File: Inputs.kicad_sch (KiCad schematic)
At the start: 6 parts, among them J26 Conn_01x04_Socket, J27 Conn_01x04_Socket, J28 Conn_01x04_Socket, J29 Conn_01x04_Socket, J30 Conn_01x02_Socket

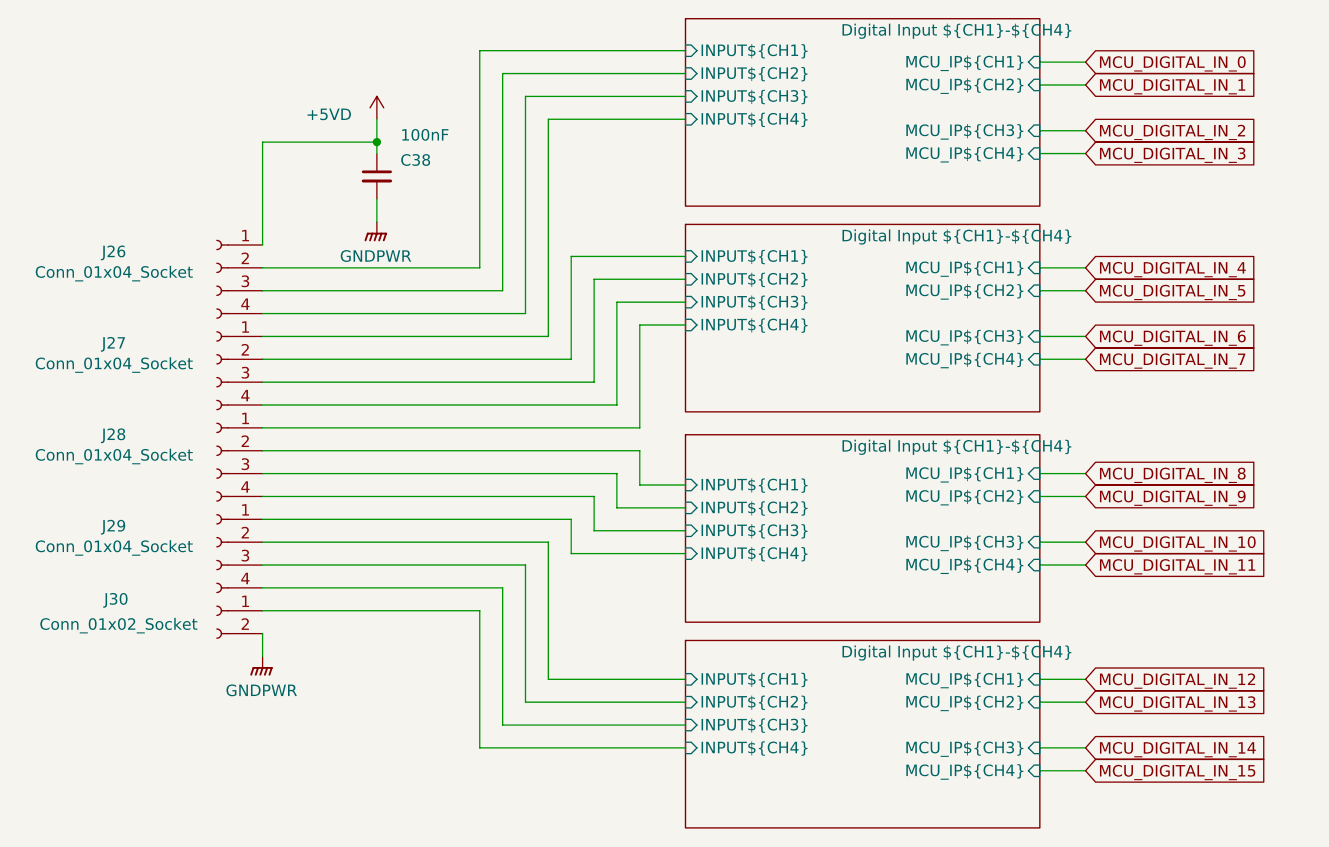
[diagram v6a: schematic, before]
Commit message: Switched terminal footprints over to a finer pitch. Corrected an issue with component reference values preventing proper use of multi channel rule areas. Component references for 4 channel optos are more straightforward as a result
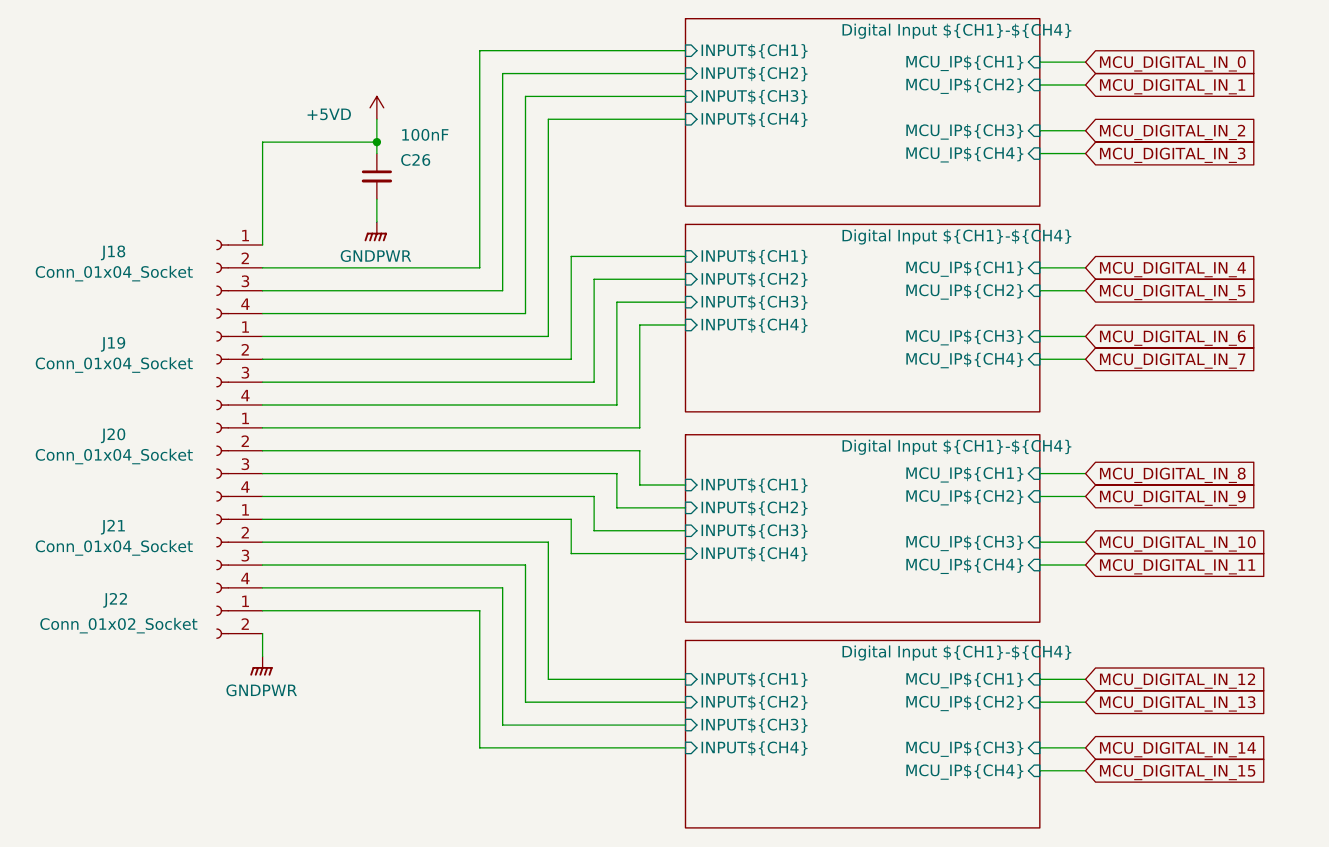
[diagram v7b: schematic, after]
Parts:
- J18: renamed from J26; footprint Amphenol QT:QT04ADP83V0000G -> 691412120004B:691412120004B; Digikey Part Number 1818-QT04ADP83V0000G-ND -> 732-691412120004B-ND; Digikey URL https://www.digikey.com.au/en/products/detail/amphenol-anyt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 -> https://www.digikey.com.au/en/products/detail/w%C3%BCrth-el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
- J19: renamed from J27; footprint Amphenol QT:QT04ADP83V0000G -> 691412120004B:691412120004B; Digikey Part Number 1818-QT04ADP83V0000G-ND -> 732-691412120004B-ND; Digikey URL https://www.digikey.com.au/en/products/detail/amphenol-anyt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 -> https://www.digikey.com.au/en/products/detail/w%C3%BCrth-el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
- J20: renamed from J28; footprint Amphenol QT:QT04ADP83V0000G -> 691412120004B:691412120004B; Digikey Part Number 1818-QT04ADP83V0000G-ND -> 732-691412120004B-ND; Digikey URL https://www.digikey.com.au/en/products/detail/amphenol-anyt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 -> https://www.digikey.com.au/en/products/detail/w%C3%BCrth-el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
- J21: renamed from J29; footprint Amphenol QT:QT04ADP83V0000G -> 691412120004B:691412120004B; Digikey Part Number 1818-QT04ADP83V0000G-ND -> 732-691412120004B-ND; Digikey URL https://www.digikey.com.au/en/products/detail/amphenol-anyt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 -> https://www.digikey.com.au/en/products/detail/w%C3%BCrth-el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
- J22: renamed from J30; footprint Amphenol QT:QT02ADP83V0000G -> 691412120002B:691412120002B; Digikey Part Number 1818-QT02ADP83V0000G-ND -> 732-691412120002B-ND; Digikey URL https://www.digikey.com.au/en/products/detail/amphenol-anyt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 -> https://www.digikey.com.au/en/products/detail/w%C3%BCrth-el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
- renumbered C38 to C26
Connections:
- net Digital Input ${CH1}-${CH4}/INPUT${CH1} is gone; now on net Digital Input ${CH1}-${CH4}/INPUT${CH1}: J19.2 (Pin_2)
- net Digital Input ${CH1}-${CH4}/INPUT${CH2} is gone; now on net Digital Input ${CH1}-${CH4}/INPUT${CH2}: J19.3 (Pin_3)
- net Digital Input ${CH1}-${CH4}/INPUT${CH3} is gone; now on net Digital Input ${CH1}-${CH4}/INPUT${CH3}: J19.4 (Pin_4)
- net Digital Input ${CH1}-${CH4}/INPUT${CH4} is gone; now on net Digital Input ${CH1}-${CH4}/INPUT${CH4}: J19.1 (Pin_1)
- net Digital Input ${CH1}-${CH4}/INPUT${CH1}: no longer J21.2 (Pin_2)
- net Digital Input ${CH1}-${CH4}/INPUT${CH2}: no longer J21.3 (Pin_3)
- net Digital Input ${CH1}-${CH4}/INPUT${CH3}: no longer J21.4 (Pin_4)
- net Digital Input ${CH1}-${CH4}/INPUT${CH4}: no longer J21.1 (Pin_1)
- new net Digital Input ${CH1}-${CH4}/INPUT${CH1}: J21.2 (Pin_2)
- new net Digital Input ${CH1}-${CH4}/INPUT${CH2}: J21.3 (Pin_3)
- new net Digital Input ${CH1}-${CH4}/INPUT${CH3}: J21.4 (Pin_4)
- new net Digital Input ${CH1}-${CH4}/INPUT${CH4}: J21.1 (Pin_1)
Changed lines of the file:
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@@
 		(on_board yes)
 		(dnp no)
-		(property "Reference" "J29"
+		(property "Reference" "J21"
 			(at 80.01 104.902 0)
 			(effects
@@
 			)
 		)
-		(property "Footprint" "Amphenol QT:QT04ADP83V0000G"
+		(property "Footprint" "691412120004B:691412120004B"
 			(at 91.44 106.68 0)
 			(effects
@@
 			)
 		)
-		(property "Digikey Part Number" "1818-QT04ADP83V0000G-ND"
+		(property "Digikey Part Number" "732-691412120004B-ND"
 			(at 91.44 106.68 0)
 			(effects
@@
 			)
 		)
-		(property "Digikey URL" "https://www.digikey.com.au/en/products/detail/amphenol-anytek/QT04ADP83V0000G/25618782"
+		(property "Digikey URL" "https://www.digikey.com.au/en/products/detail/w%C3%BCrth-elektronik/691412120004B/11478393"
 			(at 91.44 106.68 0)
 			(effects
@@
 			(project "Remora Nucleo F446ZE Hat"
 				(path "/5473abc6-7b93-43cc-a401-f691c4d7d7cf/181d5939-8311-41b3-8216-f7233e3a75eb"
-					(reference "J29")
+					(reference "J21")
 					(unit 1)
 				)
@@
 		(dnp no)
 		(fields_autoplaced yes)
-		(property "Reference" "#PWR0228"
+		(property "Reference" "#PWR0160"
 			(at 96.52 124.46 0)
 			(effects
@@
 			(project "Remora Nucleo F446ZE Hat"
 				(path "/5473abc6-7b93-43cc-a401-f691c4d7d7cf/181d5939-8311-41b3-8216-f7233e3a75eb"
-					(reference "#PWR0228")
+					(reference "#PWR0160")
 					(unit 1)
 				)
@@
 		(on_board yes)
 		(dnp no)
-		(property "Reference" "#PWR0229"
+		(property "Reference" "#PWR0161"
 			(at 109.22 63.5 0)
 			(effects
@@
 			(project "Remora Nucleo F446ZE Hat"
 				(path "/5473abc6-7b93-43cc-a401-f691c4d7d7cf/181d5939-8311-41b3-8216-f7233e3a75eb"
-					(reference "#PWR0229")
+					(reference "#PWR0161")
 					(unit 1)
 				)
@@
 		(on_board yes)
 		(dnp no)
-		(property "Reference" "J26"
+		(property "Reference" "J18"
 			(at 80.01 74.422 0)
 			(effects
@@
 			)
 		)
-		(property "Footprint" "Amphenol QT:QT04ADP83V0000G"
+		(property "Footprint" "691412120004B:691412120004B"
 			(at 91.44 76.2 0)
 			(effects
@@
 			)
 		)
-		(property "Digikey Part Number" "1818-QT04ADP83V0000G-ND"
+		(property "Digikey Part Number" "732-691412120004B-ND"
 			(at 91.44 76.2 0)
 			(effects
@@
 			)
 		)
-		(property "Digikey URL" "https://www.digikey.com.au/en/products/detail/amphenol-anytek/QT04ADP83V0000G/25618782"
+		(property "Digikey URL" "https://www.digikey.com.au/en/products/detail/w%C3%BCrth-elektronik/691412120004B/11478393"
 			(at 91.44 76.2 0)
 			(effects
@@
 			(project "Remora Nucleo F446ZE Hat"
 				(path "/5473abc6-7b93-43cc-a401-f691c4d7d7cf/181d5939-8311-41b3-8216-f7233e3a75eb"
-					(reference "J26")
+					(reference "J18")
 					(unit 1)
 				)
@@
 		(on_board yes)
 		(dnp no)
-		(property "Reference" "C38"
+		(property "Reference" "C26"
 			(at 113.538 64.262 0)
 			(effects
@@
 			(project "Remora Nucleo F446ZE Hat"
 				(path "/5473abc6-7b93-43cc-a401-f691c4d7d7cf/181d5939-8311-41b3-8216-f7233e3a75eb"
-					(reference "C38")
+					(reference "C26")
 					(unit 1)
 				)
@@
 		(dnp no)
 		(fields_autoplaced yes)
-		(property "Reference" "#PWR0230"
+		(property "Reference" "#PWR0162"
 			(at 109.22 76.2 0)
 			(effects
@@
 			(project "Remora Nucleo F446ZE Hat"
 				(path "/5473abc6-7b93-43cc-a401-f691c4d7d7cf/181d5939-8311-41b3-8216-f7233e3a75eb"
-					(reference "#PWR0230")
+					(reference "#PWR0162")
 					(unit 1)
 				)
@@
 		(on_board yes)
 		(dnp no)
-		(property "Reference" "J30"
+		(property "Reference" "J22"
 			(at 80.264 113.03 0)
 			(effects
@@
 			)
 		)
-		(property "Footprint" "Amphenol QT:QT02ADP83V0000G"
+		(property "Footprint" "691412120002B:691412120002B"
 			(at 91.44 114.3 0)
 			(effects
@@
 			)
 		)
-		(property "Digikey Part Number" "1818-QT02ADP83V0000G-ND"
+		(property "Digikey Part Number" "732-691412120002B-ND"
 			(at 91.44 114.3 0)
 			(effects
@@
 			)
 		)
-		(property "Digikey URL" "https://www.digikey.com.au/en/products/detail/amphenol-anytek/QT02ADP83V0000G/25618889"
+		(property "Digikey URL" "https://www.digikey.com.au/en/products/detail/w%C3%BCrth-elektronik/691412120002B/11478592"
 			(at 91.44 114.3 0)
 			(effects
@@
 			(project "Remora Nucleo F446ZE Hat"
 				(path "/5473abc6-7b93-43cc-a401-f691c4d7d7cf/181d5939-8311-41b3-8216-f7233e3a75eb"
-					(reference "J30")
+					(reference "J22")
 					(unit 1)
 				)
@@
 		(on_board yes)
 		(dnp no)
-		(property "Reference" "J28"
+		(property "Reference" "J20"
 			(at 80.01 94.742 0)
 			(effects
@@
 			)
 		)
-		(property "Footprint" "Amphenol QT:QT04ADP83V0000G"
+		(property "Footprint" "691412120004B:691412120004B"
 			(at 91.44 96.52 0)
 			(effects
@@
 			)
 		)
-		(property "Digikey Part Number" "1818-QT04ADP83V0000G-ND"
+		(property "Digikey Part Number" "732-691412120004B-ND"
 			(at 91.44 96.52 0)
 			(effects
@@
 			)
 		)
-		(property "Digikey URL" "https://www.digikey.com.au/en/products/detail/amphenol-anytek/QT04ADP83V0000G/25618782"
+		(property "Digikey URL" "https://www.digikey.com.au/en/products/detail/w%C3%BCrth-elektronik/691412120004B/11478393"
 			(at 91.44 96.52 0)
 			(effects
@@
 			(project "Remora Nucleo F446ZE Hat"
 				(path "/5473abc6-7b93-43cc-a401-f691c4d7d7cf/181d5939-8311-41b3-8216-f7233e3a75eb"
-					(reference "J28")
+					(reference "J20")
 					(unit 1)
 				)
@@
 		(on_board yes)
 		(dnp no)
-		(property "Reference" "J27"
+		(property "Reference" "J19"
 			(at 80.01 84.582 0)
 			(effects
@@
 			)
 		)
-		(property "Footprint" "Amphenol QT:QT04ADP83V0000G"
+		(property "Footprint" "691412120004B:691412120004B"
 			(at 91.44 86.36 0)
 			(effects
@@
 			)
 		)
-		(property "Digikey Part Number" "1818-QT04ADP83V0000G-ND"
+		(property "Digikey Part Number" "732-691412120004B-ND"
 			(at 91.44 86.36 0)
 			(effects
@@
 			)
 		)
-		(property "Digikey URL" "https://www.digikey.com.au/en/products/detail/amphenol-anytek/QT04ADP83V0000G/25618782"
+		(property "Digikey URL" "https://www.digikey.com.au/en/products/detail/w%C3%BCrth-elektronik/691412120004B/11478393"
 			(at 91.44 86.36 0)
 			(effects
@@
 			(project "Remora Nucleo F446ZE Hat"
 				(path "/5473abc6-7b93-43cc-a401-f691c4d7d7cf/181d5939-8311-41b3-8216-f7233e3a75eb"
-					(reference "J27")
-					(unit 1)
-				)
+					(reference "J19")
+					(unit 1)
+				)

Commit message: Added 3d Models for new terminal connectors for easy board verification before committing to build
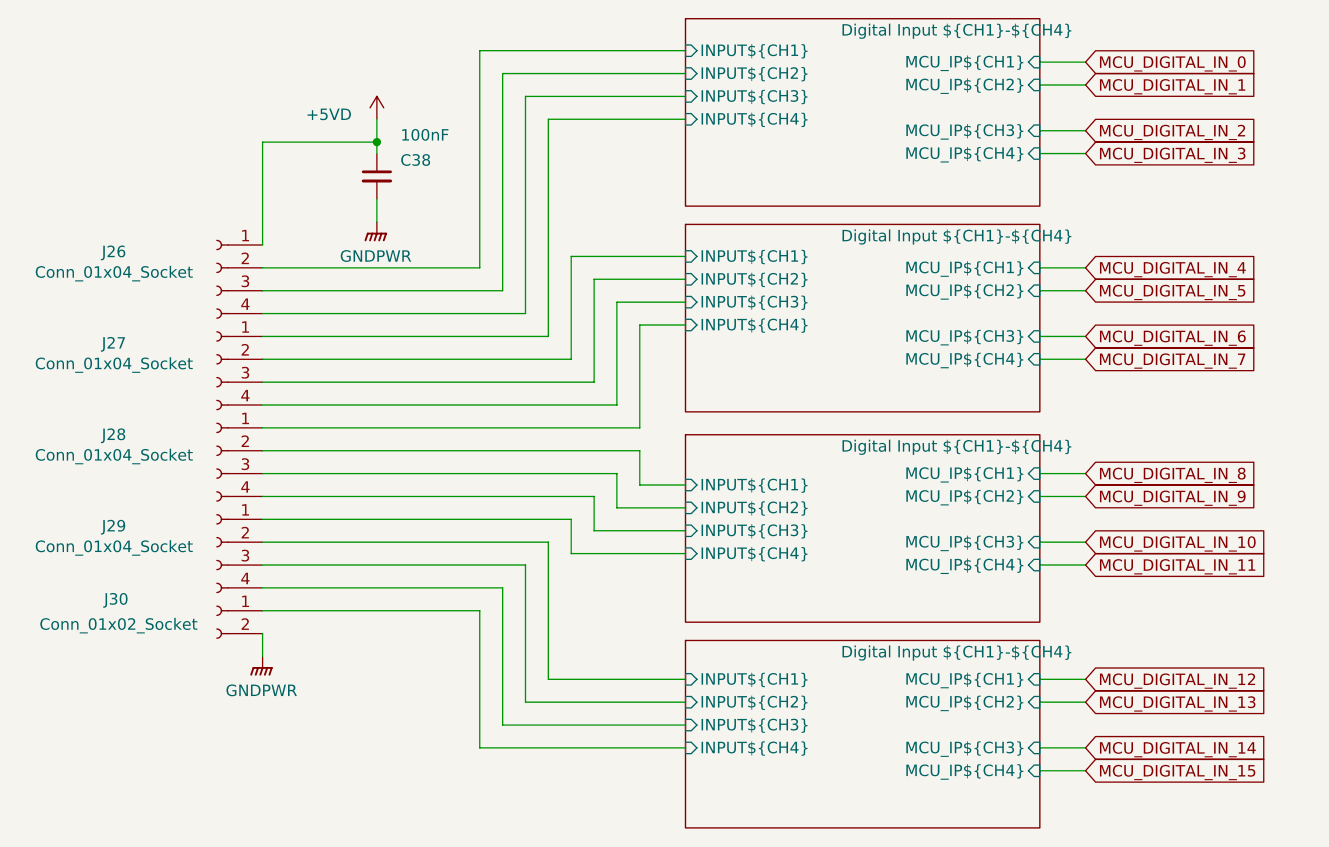
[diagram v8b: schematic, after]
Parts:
- renumbered C26 to C38, J18 to J26, J19 to J27, J20 to J28, J21 to J29, J22 to J30
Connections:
- net Digital Input ${CH1}-${CH4}/INPUT${CH1} is gone; now on net Digital Input ${CH1}-${CH4}/INPUT${CH1}: J27.2 (Pin_2)
- net Digital Input ${CH1}-${CH4}/INPUT${CH2} is gone; now on net Digital Input ${CH1}-${CH4}/INPUT${CH2}: J27.3 (Pin_3)
- net Digital Input ${CH1}-${CH4}/INPUT${CH3} is gone; now on net Digital Input ${CH1}-${CH4}/INPUT${CH3}: J27.4 (Pin_4)
- net Digital Input ${CH1}-${CH4}/INPUT${CH4} is gone; now on net Digital Input ${CH1}-${CH4}/INPUT${CH4}: J27.1 (Pin_1)
- net Digital Input ${CH1}-${CH4}/INPUT${CH1}: no longer J29.2 (Pin_2)
- net Digital Input ${CH1}-${CH4}/INPUT${CH2}: no longer J29.3 (Pin_3)
- net Digital Input ${CH1}-${CH4}/INPUT${CH3}: no longer J29.4 (Pin_4)
- net Digital Input ${CH1}-${CH4}/INPUT${CH4}: no longer J29.1 (Pin_1)
- new net Digital Input ${CH1}-${CH4}/INPUT${CH1}: J29.2 (Pin_2)
- new net Digital Input ${CH1}-${CH4}/INPUT${CH2}: J29.3 (Pin_3)
- new net Digital Input ${CH1}-${CH4}/INPUT${CH3}: J29.4 (Pin_4)
- new net Digital Input ${CH1}-${CH4}/INPUT${CH4}: J29.1 (Pin_1)
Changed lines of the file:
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@@
 		(on_board yes)
 		(dnp no)
-		(property "Reference" "J21"
+		(property "Reference" "J29"
 			(at 80.01 104.902 0)
 			(effects
@@
 			(project "Remora Nucleo F446ZE Hat"
 				(path "/5473abc6-7b93-43cc-a401-f691c4d7d7cf/181d5939-8311-41b3-8216-f7233e3a75eb"
-					(reference "J21")
+					(reference "J29")
 					(unit 1)
 				)
@@
 		(dnp no)
 		(fields_autoplaced yes)
-		(property "Reference" "#PWR0160"
+		(property "Reference" "#PWR0228"
 			(at 96.52 124.46 0)
 			(effects
@@
 			(project "Remora Nucleo F446ZE Hat"
 				(path "/5473abc6-7b93-43cc-a401-f691c4d7d7cf/181d5939-8311-41b3-8216-f7233e3a75eb"
-					(reference "#PWR0160")
+					(reference "#PWR0228")
 					(unit 1)
 				)
@@
 		(on_board yes)
 		(dnp no)
-		(property "Reference" "#PWR0161"
+		(property "Reference" "#PWR0229"
 			(at 109.22 63.5 0)
 			(effects
@@
 			(project "Remora Nucleo F446ZE Hat"
 				(path "/5473abc6-7b93-43cc-a401-f691c4d7d7cf/181d5939-8311-41b3-8216-f7233e3a75eb"
-					(reference "#PWR0161")
+					(reference "#PWR0229")
 					(unit 1)
 				)
@@
 		(on_board yes)
 		(dnp no)
-		(property "Reference" "J18"
+		(property "Reference" "J26"
 			(at 80.01 74.422 0)
 			(effects
@@
 			(project "Remora Nucleo F446ZE Hat"
 				(path "/5473abc6-7b93-43cc-a401-f691c4d7d7cf/181d5939-8311-41b3-8216-f7233e3a75eb"
-					(reference "J18")
+					(reference "J26")
 					(unit 1)
 				)
@@
 		(on_board yes)
 		(dnp no)
-		(property "Reference" "C26"
+		(property "Reference" "C38"
 			(at 113.538 64.262 0)
 			(effects
@@
 			(project "Remora Nucleo F446ZE Hat"
 				(path "/5473abc6-7b93-43cc-a401-f691c4d7d7cf/181d5939-8311-41b3-8216-f7233e3a75eb"
-					(reference "C26")
+					(reference "C38")
 					(unit 1)
 				)
@@
 		(dnp no)
 		(fields_autoplaced yes)
-		(property "Reference" "#PWR0162"
+		(property "Reference" "#PWR0230"
 			(at 109.22 76.2 0)
 			(effects
@@
 			(project "Remora Nucleo F446ZE Hat"
 				(path "/5473abc6-7b93-43cc-a401-f691c4d7d7cf/181d5939-8311-41b3-8216-f7233e3a75eb"
-					(reference "#PWR0162")
+					(reference "#PWR0230")
 					(unit 1)
 				)
@@
 		(on_board yes)
 		(dnp no)
-		(property "Reference" "J22"
+		(property "Reference" "J30"
 			(at 80.264 113.03 0)
 			(effects
@@
 			(project "Remora Nucleo F446ZE Hat"
 				(path "/5473abc6-7b93-43cc-a401-f691c4d7d7cf/181d5939-8311-41b3-8216-f7233e3a75eb"
-					(reference "J22")
+					(reference "J30")
 					(unit 1)
 				)
@@
 		(on_board yes)
 		(dnp no)
-		(property "Reference" "J20"
+		(property "Reference" "J28"
 			(at 80.01 94.742 0)
 			(effects
@@
 			(project "Remora Nucleo F446ZE Hat"
 				(path "/5473abc6-7b93-43cc-a401-f691c4d7d7cf/181d5939-8311-41b3-8216-f7233e3a75eb"
-					(reference "J20")
+					(reference "J28")
 					(unit 1)
 				)
@@
 		(on_board yes)
 		(dnp no)
-		(property "Reference" "J19"
+		(property "Reference" "J27"
 			(at 80.01 84.582 0)
 			(effects
@@
 			(project "Remora Nucleo F446ZE Hat"
 				(path "/5473abc6-7b93-43cc-a401-f691c4d7d7cf/181d5939-8311-41b3-8216-f7233e3a75eb"
-					(reference "J19")
-					(unit 1)
-				)
+					(reference "J27")
+					(unit 1)
+				)
